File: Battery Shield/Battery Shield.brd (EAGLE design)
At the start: 22.8 x 39 mm, 3 parts

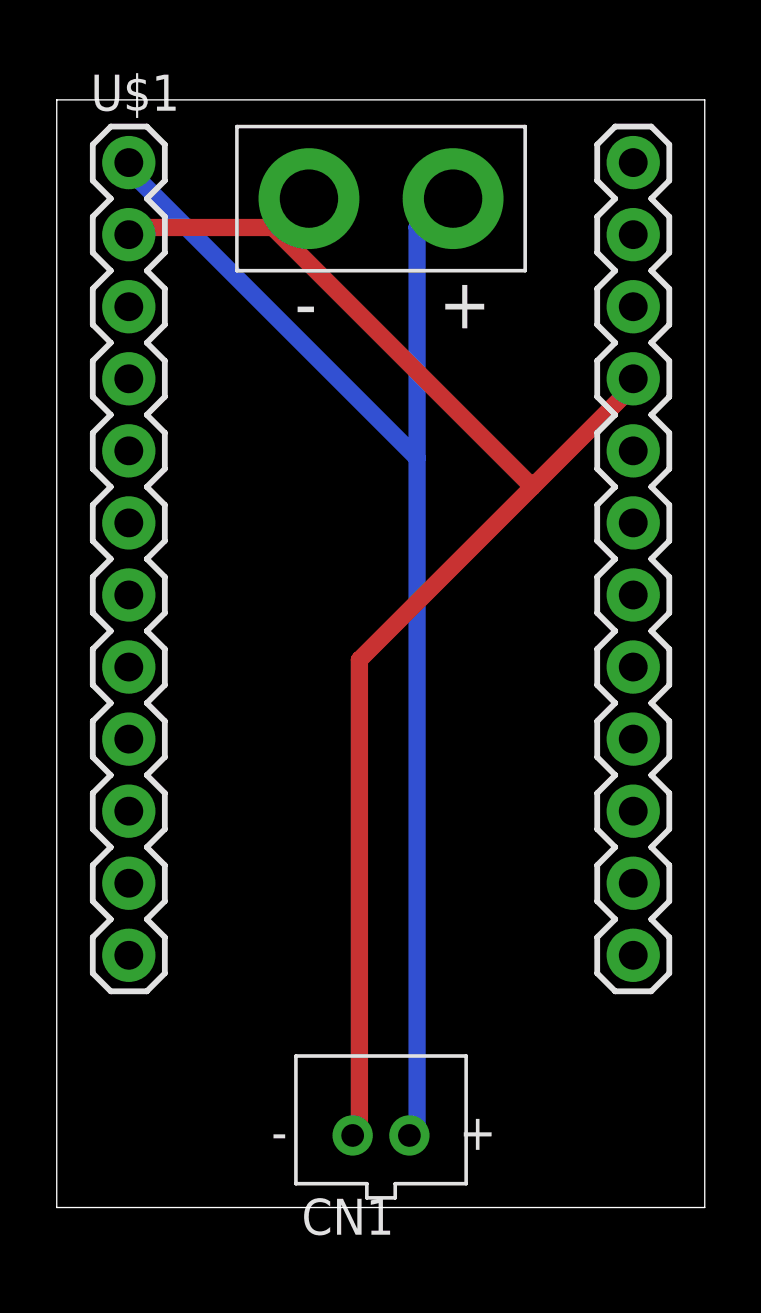
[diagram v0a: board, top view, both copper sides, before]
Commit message: Reviewed battery shield and PIR shield. Good to go.
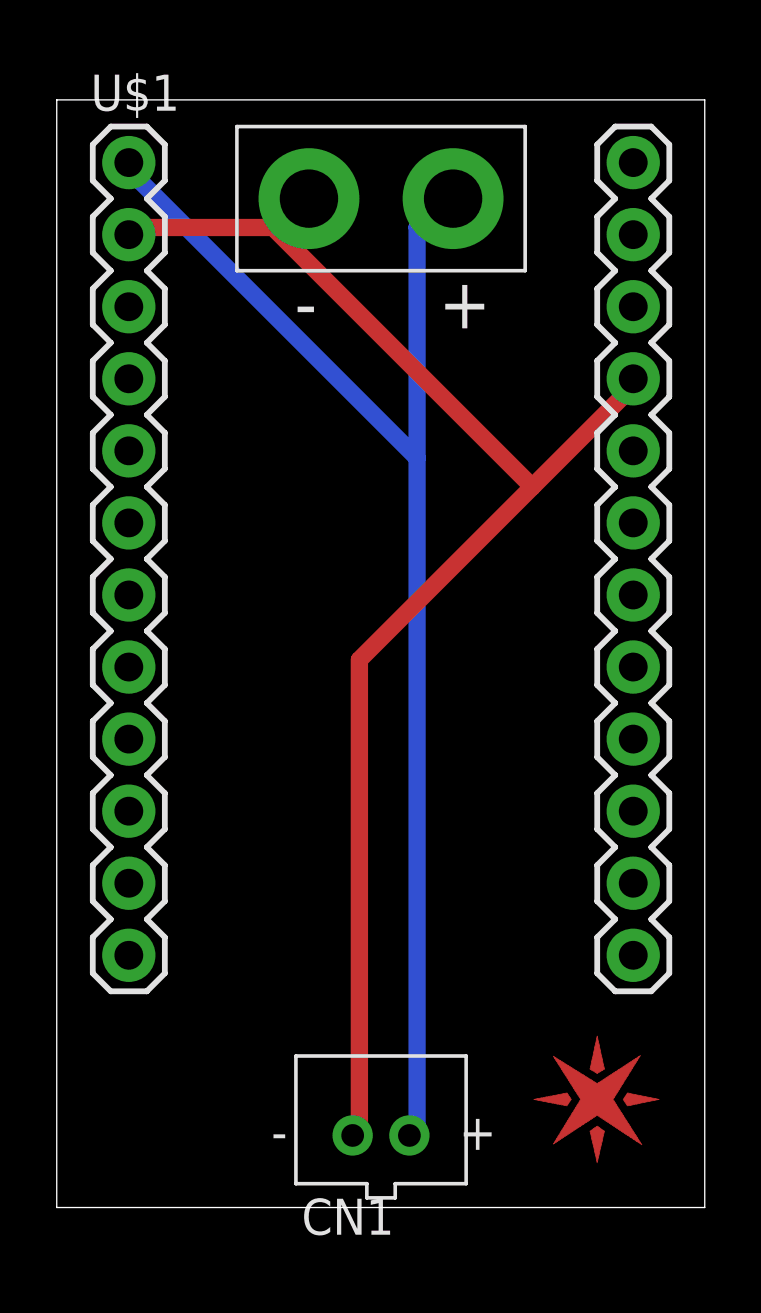
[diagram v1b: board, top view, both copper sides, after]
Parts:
- added U$2: (no value), Spark:SPARK_LOGO_PLUS_PLANE
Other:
- board text added: "Spark Battery Shield v0.1 2013-04-05"
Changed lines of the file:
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@@
 <setting verticaltext="up"/>
 </settings>
-<grid distance="0.01" unitdist="inch" unit="inch" style="lines" multiple="1" display="yes" altdistance="0.005" altunitdist="inch" altunit="inch"/>
+<grid distance="0.05" unitdist="inch" unit="inch" style="lines" multiple="1" display="yes" altdistance="0.005" altunitdist="inch" altunit="inch"/>
 <layers>
 <layer number="1" name="Top" color="4" fill="1" visible="yes" active="yes"/>
@@
 <text x="13.462" y="30.988" size="1.778" layer="21" font="vector" ratio="15">+</text>
 <text x="8.382" y="30.988" size="1.778" layer="21" font="vector" ratio="15">-</text>
+<text x="6.35" y="7.62" size="1.778" layer="22" font="vector" ratio="15" rot="MR90">Spark
+Battery Shield
+v0.1
+2013-04-05</text>
 </plain>
 <attributes>
@@
 <element name="CN1" library="adafruit" package="JST-PH-2-THM" value="" x="11.43" y="2.54"/>
 <element name="JP1" library="SparkFun-Connectors" package="1X02_XTRA_BIG" value="" x="11.43" y="35.56" rot="R180"/>
+<element name="U$2" library="Spark" package="SPARK_LOGO_PLUS_PLANE" value="" x="19.05" y="3.81"/>
 </elements>
 <signals>
@@
 </signal>
 <signal name="GND">
-<contactref element="U$1" pad="21"/>
 <contactref element="CN1" pad="2"/>
 <contactref element="U$1" pad="2"/>
@@
 <wire x1="16.764" y1="25.4" x2="10.668" y2="19.304" width="0.6096" layer="1"/>
 <wire x1="10.668" y1="2.54" x2="10.43" y2="2.54" width="0.6096" layer="1"/>
-<wire x1="20.32" y1="28.956" x2="20.32" y2="29.21" width="0.254" layer="1"/>
 <wire x1="16.764" y1="25.4" x2="7.62" y2="34.544" width="0.6096" layer="1"/>
+<contactref element="U$1" pad="21"/>
+<wire x1="20.32" y1="28.956" x2="20.32" y2="29.21" width="0" layer="19" extent="1-1"/>
 </signal>
 <signal name="RAW">
@@
 </board>
 </drawing>
+<compatibility>
+<note version="6.3" minversion="6.2.2" severity="warning">
+Since Version 6.2.2 text objects can contain more than one line,
+which will not be processed correctly with this version.
+</note>
+</compatibility>
 </eagle>
